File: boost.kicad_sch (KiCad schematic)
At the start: 0 parts

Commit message: Moved 5v boost to the boost schematic
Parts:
- added 5V1: TestPoint, TestPoint:TestPoint_Pad_2.0x2.0mm, symbol Connector:TestPoint
- added BT1: 1.5V, Battery:BatteryHolder_Keystone_2460_1xAA, symbol Device:Battery_Cell
- added C1: 10uF, Capacitor_SMD:C_0805_2012Metric_Pad1.18x1.45mm_HandSolder, symbol Device:C
- added C2, C3: 22uF, Capacitor_SMD:C_0805_2012Metric_Pad1.18x1.45mm_HandSolder, symbol Device:C
- added L1: 470nH, Inductor_SMD:L_Coilcraft_XxL4020, symbol Device:L
- added R1: 100K, Resistor_SMD:R_0805_2012Metric_Pad1.20x1.40mm_HandSolder, symbol Device:R_US
- added R2: 806K, Resistor_SMD:R_0805_2012Metric_Pad1.20x1.40mm_HandSolder, symbol Device:R_US
- added R3: 91K, Resistor_SMD:R_0805_2012Metric_Pad1.20x1.40mm_HandSolder, symbol Device:R_US
- added U1: TPS63802DLAR, TPS63802DLAR:DLA0010A, symbol TPS63802DLAR:TPS63802DLAR
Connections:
- new net: BT1.1 (+), C1.1, U1.1 (EN), U1.10 (VIN)
- new net: R2.1, R3.2, U1.4 (FB)
- new net: R1.1, U1.5 (PG)
- new net: L1.2, U1.7 (L2)
- new net: L1.1, U1.9 (L1)
- new net 5V: 5V1.1, C2.1, C3.1, R1.2, R2.2, U1.6 (VOUT)
- new net GND: BT1.2 (-), C1.2, C2.2, C3.2, R3.1, U1.2 (MODE), U1.3 (AGND), U1.8 (GND)

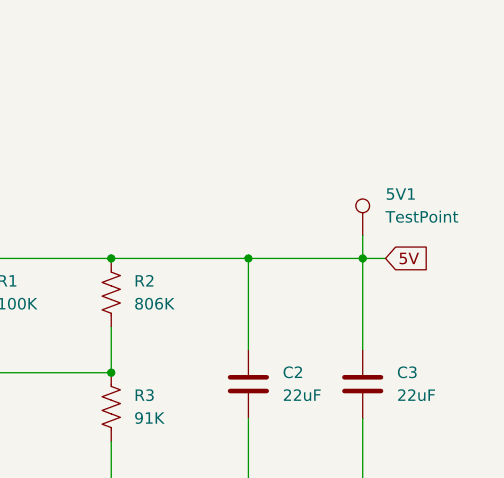
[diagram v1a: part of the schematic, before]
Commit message: Finished rotary switch and updated MCU pinout
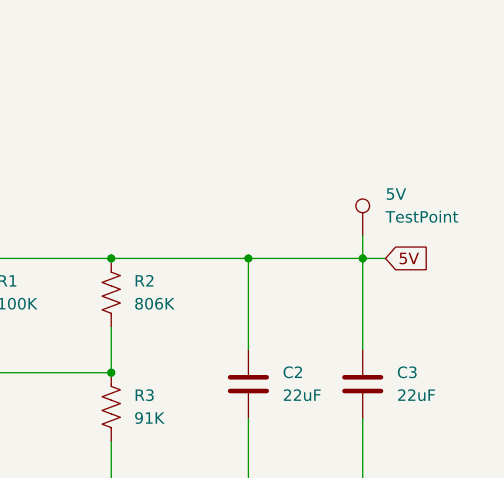
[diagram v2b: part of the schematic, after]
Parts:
- L1: footprint Inductor_SMD:L_Coilcraft_XxL4020 -> DFE201612P-470nH:INDC2016X120N
- renumbered 5V1 to 5V
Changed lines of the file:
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@@
 			)
 		)
-		(property "Footprint" "Inductor_SMD:L_Coilcraft_XxL4020"
+		(property "Footprint" "DFE201612P-470nH:INDC2016X120N"
 			(at 101.6 43.18 0)
 			(effects
@@
 		(dnp no)
 		(fields_autoplaced yes)
-		(property "Reference" "5V1"
+		(property "Reference" "5V"
 			(at 172.72 56.3879 0)
 			(effects
@@
 			(project "FES_Hardware"
 				(path "/225cfa82-97e7-4320-90e1-4d94ef39f9f2/cd32b677-73b6-40f3-905a-e4b052fd72c9"
-					(reference "5V1")
-					(unit 1)
-				)
+					(reference "5V")
+					(unit 1)
+				)

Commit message: Updated references after merging
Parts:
- renumbered C1 to C6, C2 to C7, C3 to C8, L1 to L2, R3 to R10, R1 to R8, R2 to R9, U1 to U2
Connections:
- net 5V renamed +5V

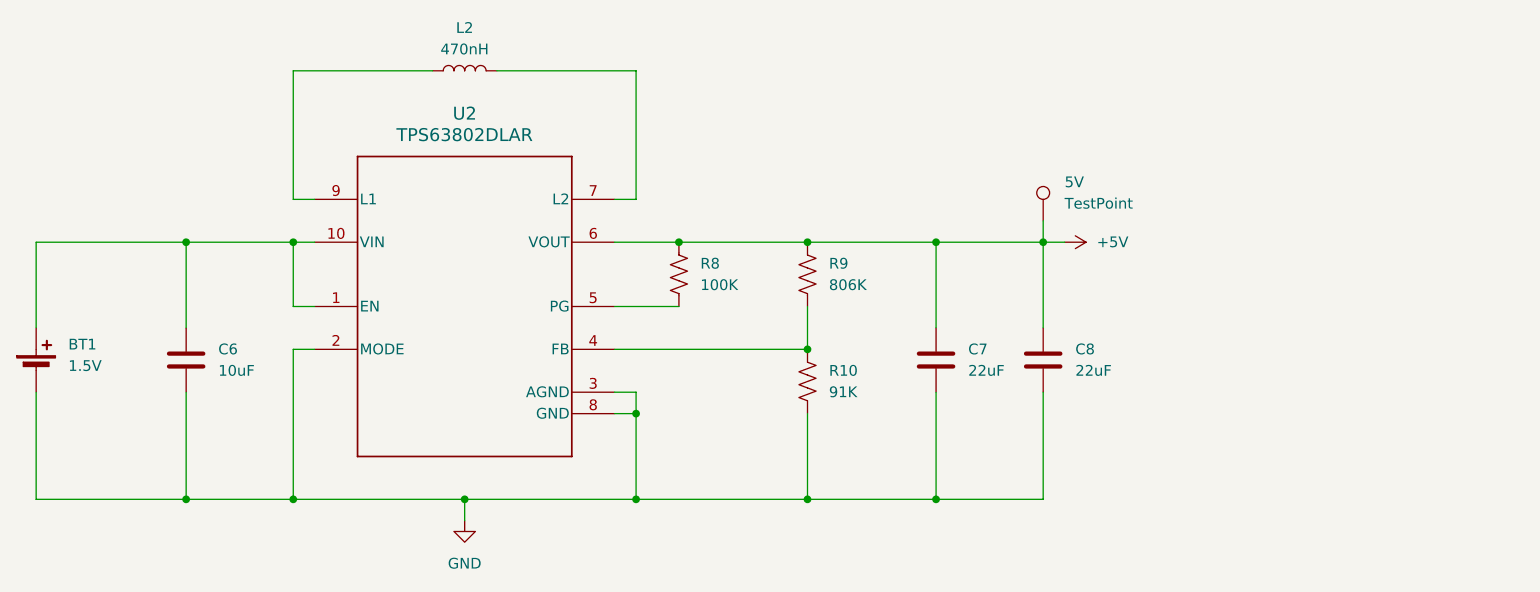
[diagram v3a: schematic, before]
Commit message: Updated footprints of passive elements to be 0805 Hand-Solder
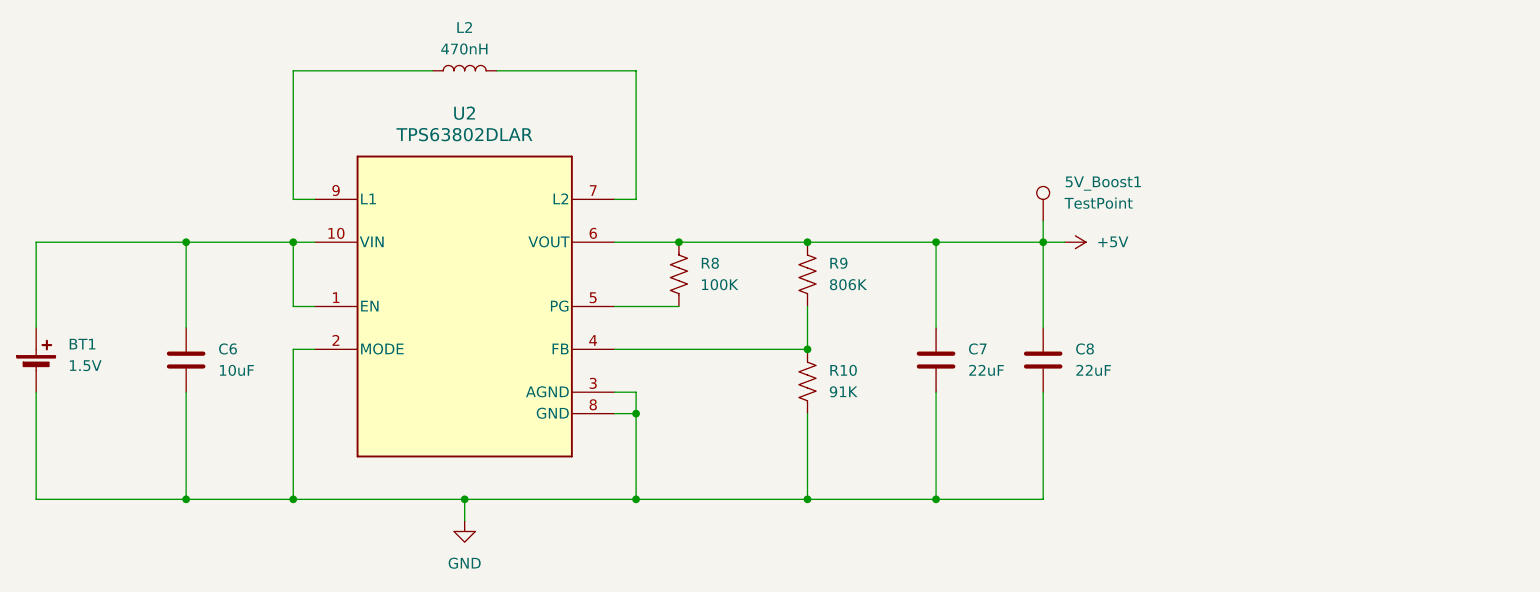
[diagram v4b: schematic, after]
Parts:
- 5V_Boost1: renamed from 5V; footprint TestPoint:TestPoint_Pad_2.0x2.0mm -> TestPoint:TestPoint_Keystone_5019_Minature
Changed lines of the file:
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@@
 		)
 		(property "Footprint" "TPS63802DLAR:DLA0010A"
-			(at 101.6 71.12 0)
+			(at 101.854 87.122 0)
 			(effects
 				(font
@@
 		)
 		(property "Datasheet" "TPS63802DLAR"
-			(at 101.6 71.12 0)
+			(at 101.6 55.626 0)
 			(effects
 				(font
@@
 		(dnp no)
 		(fields_autoplaced yes)
-		(property "Reference" "5V"
+		(property "Reference" "5V_Boost1"
 			(at 172.72 56.3879 0)
 			(effects
@@
 			)
 		)
-		(property "Footprint" "TestPoint:TestPoint_Pad_2.0x2.0mm"
+		(property "Footprint" "TestPoint:TestPoint_Keystone_5019_Minature"
 			(at 175.26 60.96 0)
 			(effects
@@
 			(project "FES_Hardware"
 				(path "/225cfa82-97e7-4320-90e1-4d94ef39f9f2/cd32b677-73b6-40f3-905a-e4b052fd72c9"
-					(reference "5V")
-					(unit 1)
-				)
+					(reference "5V_Boost1")
+					(unit 1)
+				)

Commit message: commiting unsaved changes
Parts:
- added D6: LED, LED_SMD:LED_0805_2012Metric_Pad1.15x1.40mm_HandSolder, symbol Device:LED
- added R22: 150, Resistor_SMD:R_0805_2012Metric_Pad1.20x1.40mm_HandSolder, symbol Device:R_US
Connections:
- net +5V: now also R22.1
- net GND: now also D6.1 (K)
- new net: D6.2 (A), R22.2
